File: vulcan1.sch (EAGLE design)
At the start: 56 parts, among them Q1 IRF540, Q2 IRF540, T1 2N3904, T2 2N3904

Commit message: final changes
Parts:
- removed U$9: 1X2BIG, vulcan-1:1X2BIG
- added JP4, JP5: M025MM, SparkFun-Connectors:M025MM
- U$8: value 1X2BIG -> 1X2HEADER; device vulcan-1:1X2BIG -> 1x2 header:1X2HEADER
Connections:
- new net N$22: U$3.PB3, U$8.0
- new net N$23: U$3.PB4, U$8.1
- net N$13: now also JP4.2; no longer U$9.2
- net N$17: now also JP5.1; no longer U$8.2
- net VBAT-F: now also JP4.1, JP5.2; no longer U$8.1, U$9.1
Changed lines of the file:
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@@
 <part name="R7" library="adafruit" deviceset="R-US_" device="0204/7" value="10k"/>
 <part name="GND18" library="supply1" deviceset="GND" device=""/>
-<part name="U$9" library="vulcan-1" deviceset="1X2BIG" device=""/>
 <part name="Q1" library="transistor-power" deviceset="IRF540" device=""/>
 <part name="T1" library="transistor" deviceset="2N3904" device=""/>
 <part name="R6" library="adafruit" deviceset="R-US_" device="0204/7" value="10k"/>
 <part name="GND19" library="supply1" deviceset="GND" device=""/>
-<part name="U$8" library="vulcan-1" deviceset="1X2BIG" device=""/>
 <part name="FUSE" library="adafruit" deviceset="R-US_" device="0204/7" value="FUSE"/>
 <part name="C14" library="adafruit" deviceset="C-US" device="025-030X050" value=".1u"/>
@@
 <part name="GND20" library="supply1" deviceset="GND" device=""/>
 <part name="U$1" library="vulcan-1" deviceset="SMA" device=""/>
+<part name="JP4" library="SparkFun-Connectors" deviceset="M02" device="5MM"/>
+<part name="JP5" library="SparkFun-Connectors" deviceset="M02" device="5MM"/>
+<part name="U$8" library="1x2 header" deviceset="1X2HEADER" device=""/>
 </parts>
 <sheets>
@@
 <instance part="R7" gate="G$1" x="-2.54" y="152.4" rot="R90"/>
 <instance part="GND18" gate="1" x="2.54" y="116.84"/>
-<instance part="U$9" gate="G$1" x="15.24" y="147.32"/>
 <instance part="Q1" gate="G$1" x="35.56" y="142.24"/>
 <instance part="T1" gate="G1" x="30.48" y="129.54"/>
 <instance part="R6" gate="G$1" x="33.02" y="152.4" rot="R90"/>
 <instance part="GND19" gate="1" x="38.1" y="116.84"/>
-<instance part="U$8" gate="G$1" x="50.8" y="147.32"/>
 <instance part="FUSE" gate="G$1" x="-134.62" y="152.4" rot="R90"/>
 <instance part="C14" gate="G$1" x="-96.52" y="96.52"/>
@@
 <instance part="GND20" gate="1" x="53.34" y="33.02"/>
 <instance part="U$1" gate="G$1" x="144.78" y="5.08"/>
+<instance part="JP4" gate="G$1" x="17.78" y="149.86" rot="R180"/>
+<instance part="JP5" gate="G$1" x="53.34" y="149.86" rot="R180"/>
+<instance part="U$8" gate="G$1" x="48.26" y="12.7"/>
 </instances>
 <busses>
@@
 <segment>
 <pinref part="Q2" gate="G$1" pin="D"/>
-<pinref part="U$9" gate="G$1" pin="2"/>
 <wire x1="2.54" y1="147.32" x2="10.16" y2="147.32" width="0.1524" layer="91"/>
+<pinref part="JP4" gate="G$1" pin="2"/>
 </segment>
 </net>
@@
 </segment>
 </net>
-<net name="N$17" class="0">
-<segment>
-<pinref part="Q1" gate="G$1" pin="D"/>
-<pinref part="U$8" gate="G$1" pin="2"/>
-<wire x1="38.1" y1="147.32" x2="45.72" y2="147.32" width="0.1524" layer="91"/>
-</segment>
-</net>
 <net name="EMATCH2" class="0">
 <segment>
@@
 </segment>
 <segment>
-<pinref part="U$8" gate="G$1" pin="1"/>
-<wire x1="45.72" y1="149.86" x2="45.72" y2="157.48" width="0.1524" layer="91"/>
 <pinref part="R6" gate="G$1" pin="2"/>
-<wire x1="45.72" y1="157.48" x2="33.02" y2="157.48" width="0.1524" layer="91"/>
-<pinref part="U$9" gate="G$1" pin="1"/>
 <wire x1="10.16" y1="149.86" x2="10.16" y2="157.48" width="0.1524" layer="91"/>
 <pinref part="R7" gate="G$1" pin="2"/>
 <wire x1="10.16" y1="157.48" x2="-2.54" y2="157.48" width="0.1524" layer="91"/>
 <wire x1="33.02" y1="157.48" x2="10.16" y2="157.48" width="0.1524" layer="91"/>
-<junction x="33.02" y="157.48"/>
 <junction x="10.16" y="157.48"/>
 <wire x1="-2.54" y1="157.48" x2="-20.32" y2="157.48" width="0.1524" layer="91"/>
 <junction x="-2.54" y="157.48"/>
 <label x="-20.32" y="157.48" size="1.778" layer="95"/>
+<pinref part="JP4" gate="G$1" pin="1"/>
+<wire x1="33.02" y1="157.48" x2="40.64" y2="157.48" width="0.1524" layer="91"/>
+<junction x="33.02" y="157.48"/>
+<wire x1="40.64" y1="157.48" x2="40.64" y2="147.32" width="0.1524" layer="91"/>
+<pinref part="JP5" gate="G$1" pin="2"/>
+<wire x1="40.64" y1="147.32" x2="45.72" y2="147.32" width="0.1524" layer="91"/>
 </segment>
 </net>
@@
 </segment>
 </net>
+<net name="N$17" class="0">
+<segment>
+<pinref part="Q1" gate="G$1" pin="D"/>
+<wire x1="38.1" y1="147.32" x2="38.1" y2="149.86" width="0.1524" layer="91"/>
+<pinref part="JP5" gate="G$1" pin="1"/>
+<wire x1="38.1" y1="149.86" x2="45.72" y2="149.86" width="0.1524" layer="91"/>
+</segment>
+</net>
+<net name="N$22" class="0">
+<segment>
+<pinref part="U$3" gate="G$1" pin="PB3"/>
+<wire x1="22.86" y1="15.24" x2="43.18" y2="15.24" width="0.1524" layer="91"/>
+<pinref part="U$8" gate="G$1" pin="0"/>
+</segment>
+</net>
+<net name="N$23" class="0">
+<segment>
+<pinref part="U$3" gate="G$1" pin="PB4"/>
+<wire x1="43.18" y1="12.7" x2="22.86" y2="12.7" width="0.1524" layer="91"/>
+<pinref part="U$8" gate="G$1" pin="1"/>
+</segment>
+</net>

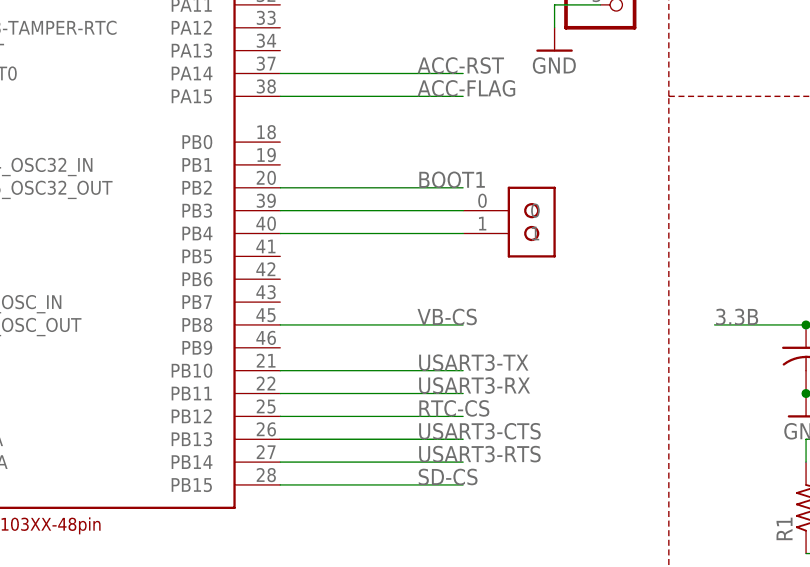
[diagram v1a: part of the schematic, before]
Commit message: clearance changed to 8mil
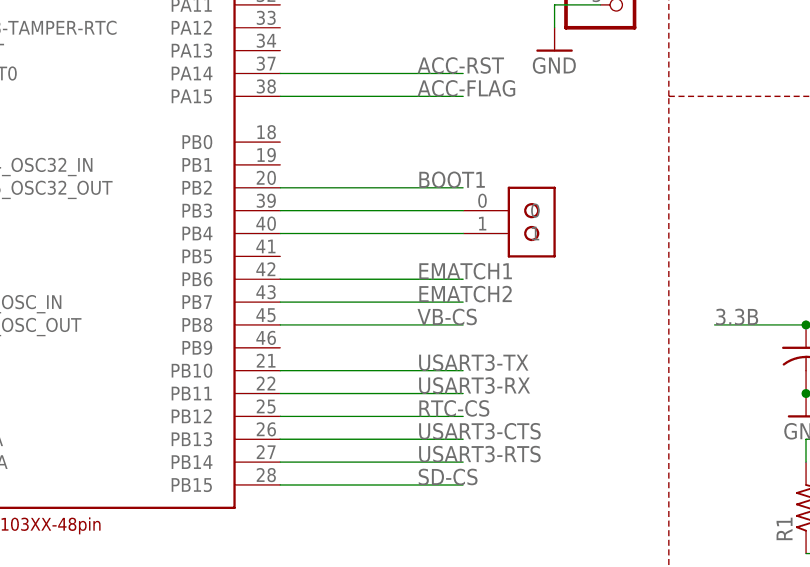
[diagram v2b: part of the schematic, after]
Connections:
- net EMATCH1: now also U$3.PB6
- net EMATCH2: now also U$3.PB7
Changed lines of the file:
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@@
 <?xml version="1.0" encoding="utf-8"?>
 <!DOCTYPE eagle SYSTEM "eagle.dtd">
-<eagle version="7.2.0">
+<eagle version="7.1.0">
 <drawing>
 <settings>
@@
 <label x="-20.32" y="129.54" size="1.778" layer="95"/>
 </segment>
+<segment>
+<pinref part="U$3" gate="G$1" pin="PB6"/>
+<wire x1="22.86" y1="7.62" x2="43.18" y2="7.62" width="0.1524" layer="91"/>
+<label x="38.1" y="7.62" size="1.778" layer="95"/>
+</segment>
 </net>
 <net name="N$16" class="0">
@@
 <wire x1="27.94" y1="129.54" x2="15.24" y2="129.54" width="0.1524" layer="91"/>
 <label x="15.24" y="129.54" size="1.778" layer="95"/>
+</segment>
+<segment>
+<pinref part="U$3" gate="G$1" pin="PB7"/>
+<wire x1="22.86" y1="5.08" x2="43.18" y2="5.08" width="0.1524" layer="91"/>
+<label x="38.1" y="5.08" size="1.778" layer="95"/>
 </segment>
 </net>
@@
 </sheet>
 </sheets>
+<errors>
+</errors>
 </schematic>
 </drawing>
